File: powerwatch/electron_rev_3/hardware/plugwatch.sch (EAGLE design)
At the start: 121 parts, among them J1 DM3AT-SF-PEJM5, J2 TC2030-JLINK-NL, U1 BGA725L6-ALT, U10 SIP32510, U11 SIP32510, U12 SIP32510, U13 SIP32510, U14 MPU-9250, U15 OPA322AIDBVT, U2 SAFFB1G56KB0F0A, U3 ISL29035, U4 MAX-M8, U5 MAX740XESA, U6 SIP32510, U7 NRF51822QF, U8 OPA322AIDBVT, U9 SIP32510, X1 32.768k, X2 16MHz

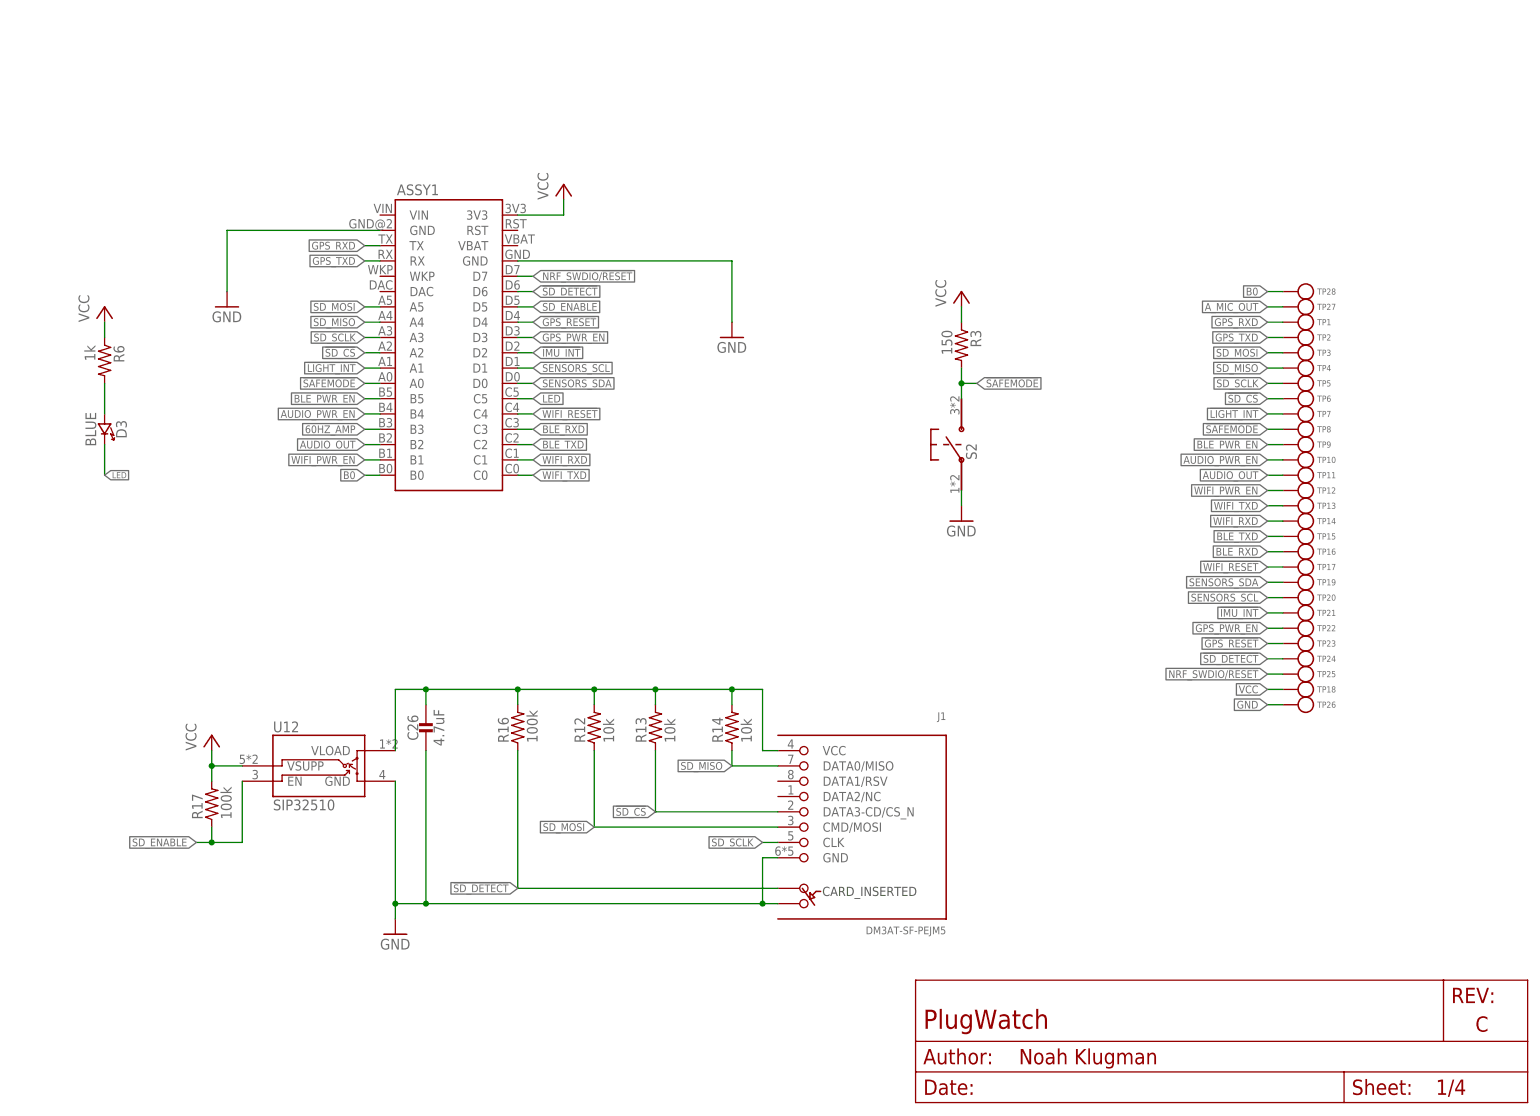
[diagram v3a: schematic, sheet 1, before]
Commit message: added in dip switch, 1-wire serial number, removed rc filter
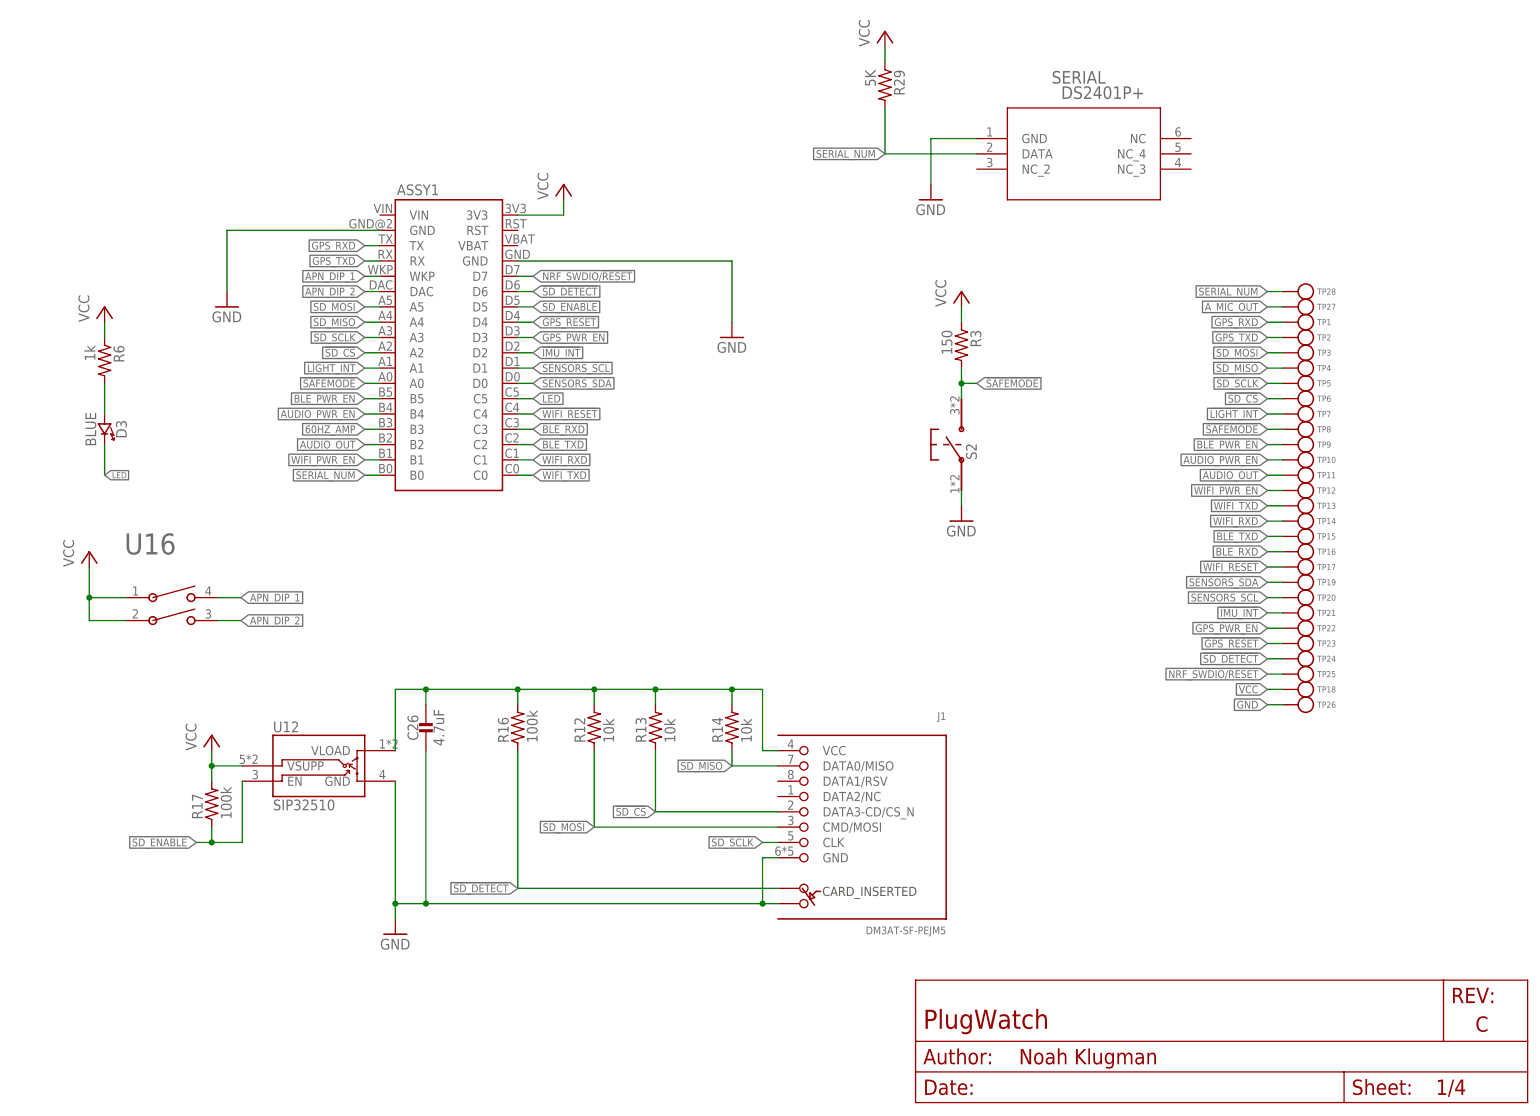
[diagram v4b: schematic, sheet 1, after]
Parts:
- removed C24: 2.2uF, passives:CAP_POL1206
- removed R24: 100k, passives:RESISTOR0603_RES
- added R29: 5K, passives:RESISTOR0402_RES
- added SERIAL: DS2401P+, DS2401P+:DS2401P+
- added U16: 1825057-1, 18250571:1825057-1
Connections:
- removed net B0: ASSY1.B0, TP28.TESTPOINT
- new net APN_DIP_1: ASSY1.WKP, U16.4
- new net APN_DIP_2: ASSY1.DAC, U16.3
- new net SERIAL_NUM: ASSY1.B0, R29.2, SERIAL.DATA, TP28.TESTPOINT
- net A_MIC_OUT: no longer C24.ANODE, R24.2
- net GND: now also SERIAL.GND; no longer R24.1
- net N$7: no longer C24.CATHODE
- net VCC: now also R29.1, U16.1, U16.2
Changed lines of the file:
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@@
 <?xml version="1.0" encoding="utf-8"?>
 <!DOCTYPE eagle SYSTEM "eagle.dtd">
-<eagle version="8.6.3">
+<eagle version="8.5.1">
 <drawing>
 <settings>
@@
 <setting verticaltext="up"/>
 </settings>
-<grid distance="0.1" unitdist="inch" unit="inch" style="lines" multiple="1" display="yes" altdistance="0.05" altunitdist="inch" altunit="inch"/>
+<grid distance="0.1" unitdist="inch" unit="inch" style="lines" multiple="1" display="no" altdistance="0.01" altunitdist="inch" altunit="inch"/>
 <layers>
 <layer number="1" name="Top" color="4" fill="1" visible="no" active="no"/>
@@
 <attribute name="MPN" value="293D225X9016A2TE3"/>
 </part>
-<part name="C24" library="passives" deviceset="CAP_POL" device="1206" value="2.2uF">
-<attribute name="DESCRIPTION" value="CAP TANT 2.2UF 16V 10% 1206"/>
-<attribute name="DIGIKEY" value="718-1131-1-ND"/>
-<attribute name="MANUFACTURER" value="Vishay"/>
-<attribute name="MPN" value="293D225X9016A2TE3"/>
-</part>
 <part name="C25" library="passives" deviceset="CAPACITOR" device="0402_CAP" value="4.7uF">
 <attribute name="DESCRIPTION" value="CAP CER 4.7UF 6.3V X5R 0402"/>
@@
 <part name="GND11" library="supply1" deviceset="GND" device=""/>
 <part name="GND12" library="SparkFun-Aesthetics" deviceset="GND" device=""/>
-<part name="GND13" library="supply1" deviceset="GND" device=""/>
 <part name="GND14" library="supply1" deviceset="GND" device=""/>
 <part name="GND15" library="supply1" deviceset="GND" device=""/>
@@
 </part>
 <part name="R23" library="passives" deviceset="RESISTOR" device="0603_RES" value="100k">
-<attribute name="DESCRIPTION" value="RES SMD 100K OHM 1% 1/10W 0603"/>
-<attribute name="DIGIKEY" value="541-2972-1-ND"/>
-<attribute name="MANUFACTURER" value="Vishay"/>
-<attribute name="MPN" value="CRCW0603100KFKEB"/>
-</part>
-<part name="R24" library="passives" deviceset="RESISTOR" device="0603_RES" value="100k">
 <attribute name="DESCRIPTION" value="RES SMD 100K OHM 1% 1/10W 0603"/>
 <attribute name="DIGIKEY" value="541-2972-1-ND"/>
@@
 <attribute name="MPN" value="8Y-16.000MAAV-T"/>
 </part>
+<part name="SERIAL" library="DS2401P+" deviceset="DS2401P+" device=""/>
+<part name="P+4" library="supply1" deviceset="VCC" device=""/>
+<part name="R29" library="passives" deviceset="RESISTOR" device="0402_RES" value="5K">
+<attribute name="DESCRIPTION" value="RES SMD 150 OHM 1% 1/16W 0402"/>
+<attribute name="DIGIKEY" value="RMCF0402FT150RCT-ND"/>
+<attribute name="MANUFACTURER" value="Stackpole Electronics"/>
+<attribute name="MPN" value="RMCF0402FT150R"/>
+</part>
+<part name="GND41" library="supply1" deviceset="GND" device=""/>
+<part name="U16" library="18250571" deviceset="1825057-1" device=""/>
+<part name="P+6" library="supply1" deviceset="VCC" device=""/>
 </parts>
 <sheets>
@@
 <instance part="TP9" gate="G$1" x="215.9" y="109.22" rot="R180"/>
 <instance part="U12" gate="G$1" x="45.72" y="48.26"/>
+<instance part="SERIAL" gate="A" x="160.02" y="160.02"/>
+<instance part="P+4" gate="VCC" x="147.32" y="177.8"/>
+<instance part="R29" gate="G$1" x="147.32" y="167.64" rot="R270">
+<attribute name="DIGIKEY" x="147.32" y="167.64" size="1.27" layer="96" rot="R270" display="off"/>
+</instance>
+<instance part="GND41" gate="1" x="154.94" y="149.86"/>
+<instance part="U16" gate="A" x="21.336" y="83.82"/>
+<instance part="P+6" gate="VCC" x="15.24" y="91.44"/>
 </instances>
 <busses>
@@
 <wire x1="213.36" y1="132.08" x2="210.82" y2="132.08" width="0.1524" layer="91"/>
 <label x="210.82" y="132.08" size="1.27" layer="95" rot="R180" xref="yes"/>
-</segment>
-</net>
-<net name="B0" class="0">
-<segment>
-<pinref part="TP28" gate="G$1" pin="TESTPOINT"/>
-<wire x1="213.36" y1="134.62" x2="210.82" y2="134.62" width="0.1524" layer="91"/>
-<label x="210.82" y="134.62" size="1.27" layer="95" rot="R180" xref="yes"/>
-</segment>
-<segment>
-<pinref part="ASSY1" gate="A1" pin="B0"/>
-<wire x1="63.5" y1="104.14" x2="60.96" y2="104.14" width="0.1524" layer="91"/>
-<label x="60.96" y="104.14" size="1.27" layer="95" rot="R180" xref="yes"/>
 </segment>
 </net>
@@
 <wire x1="213.36" y1="66.04" x2="210.82" y2="66.04" width="0.1524" layer="91"/>
 <label x="210.82" y="66.04" size="1.27" layer="95" rot="R180" xref="yes"/>
+</segment>
+<segment>
+<pinref part="SERIAL" gate="A" pin="GND"/>
+<pinref part="GND41" gate="1" pin="GND"/>
+<wire x1="162.56" y1="160.02" x2="154.94" y2="160.02" width="0.1524" layer="91"/>
+<wire x1="154.94" y1="160.02" x2="154.94" y2="152.4" width="0.1524" layer="91"/>
 </segment>
 </net>
@@
 <label x="210.82" y="68.58" size="1.27" layer="95" rot="R180" xref="yes"/>
 </segment>
+<segment>
+<pinref part="R29" gate="G$1" pin="1"/>
+<pinref part="P+4" gate="VCC" pin="VCC"/>
+<wire x1="147.32" y1="172.72" x2="147.32" y2="175.26" width="0.1524" layer="91"/>
+</segment>
+<segment>
+<pinref part="U16" gate="A" pin="1"/>
+<wire x1="21.336" y1="83.82" x2="15.24" y2="83.82" width="0.1524" layer="91"/>
+<wire x1="15.24" y1="83.82" x2="15.24" y2="88.9" width="0.1524" layer="91"/>
+<wire x1="15.24" y1="83.82" x2="15.24" y2="80.01" width="0.1524" layer="91"/>
+<wire x1="15.24" y1="80.01" x2="21.336" y2="80.01" width="0.1524" layer="91"/>
+<pinref part="U16" gate="A" pin="2"/>
+<junction x="15.24" y="83.82"/>
+<pinref part="P+6" gate="VCC" pin="VCC"/>
+</segment>
 </net>
 <net name="WIFI_PWR_EN" class="0">
@@
 <wire x1="213.36" y1="99.06" x2="210.82" y2="99.06" width="0.1524" layer="91"/>
 <label x="210.82" y="99.06" size="1.27" layer="95" rot="R180" xref="yes"/>
+</segment>
+</net>
+<net name="APN_DIP_1" class="0">
+<segment>
+<pinref part="ASSY1" gate="A1" pin="WKP"/>
+<wire x1="63.5" y1="137.16" x2="60.96" y2="137.16" width="0.1524" layer="91"/>
+<label x="60.96" y="137.16" size="1.27" layer="95" rot="R180" xref="yes"/>
+</segment>
+<segment>
+<pinref part="U16" gate="A" pin="4"/>
+<wire x1="36.576" y1="83.82" x2="40.386" y2="83.82" width="0.1524" layer="91"/>
+<label x="40.386" y="83.82" size="1.27" layer="95" xref="yes"/>
+</segment>
+</net>
+<net name="APN_DIP_2" class="0">
+<segment>
+<pinref part="ASSY1" gate="A1" pin="DAC"/>
+<wire x1="63.5" y1="134.62" x2="60.96" y2="134.62" width="0.1524" layer="91"/>
+<label x="60.96" y="134.62" size="1.27" layer="95" rot="R180" xref="yes"/>
+</segment>
+<segment>
+<pinref part="U16" gate="A" pin="3"/>
+<wire x1="36.576" y1="80.01" x2="40.386" y2="80.01" width="0.1524" layer="91"/>
+<label x="40.386" y="80.01" size="1.27" layer="95" xref="yes"/>
+</segment>
+</net>
+<net name="SERIAL_NUM" class="0">
+<segment>
+<pinref part="ASSY1" gate="A1" pin="B0"/>
+<wire x1="63.5" y1="104.14" x2="60.96" y2="104.14" width="0.1524" layer="91"/>
+<label x="60.96" y="104.14" size="1.27" layer="95" rot="R180" xref="yes"/>
+</segment>
+<segment>
+<pinref part="TP28" gate="G$1" pin="TESTPOINT"/>
+<wire x1="213.36" y1="134.62" x2="210.82" y2="134.62" width="0.1524" layer="91"/>
+<label x="210.82" y="134.62" size="1.27" layer="95" rot="R180" xref="yes"/>
+</segment>
+<segment>
+<pinref part="SERIAL" gate="A" pin="DATA"/>
+<wire x1="162.56" y1="157.48" x2="147.32" y2="157.48" width="0.1524" layer="91"/>
+<pinref part="R29" gate="G$1" pin="2"/>
+<wire x1="147.32" y1="157.48" x2="147.32" y2="165.1" width="0.1524" layer="91"/>
+<label x="147.32" y="157.48" size="1.27" layer="95" rot="R180" xref="yes"/>
 </segment>
 </net>
@@
 <attribute name="DIGIKEY" x="60.96" y="119.38" size="1.778" layer="96" display="off"/>
 </instance>
-<instance part="C24" gate="G$1" x="106.68" y="137.16" rot="R90">
-<attribute name="DIGIKEY" x="106.68" y="137.16" size="1.778" layer="96" rot="R90" display="off"/>
-</instance>
 <instance part="C28" gate="G$1" x="48.26" y="139.7" rot="R270">
 <attribute name="DIGIKEY" x="48.26" y="139.7" size="1.778" layer="96" rot="R270" display="off"/>
@@
 <instance part="GND11" gate="1" x="53.34" y="109.22"/>
 <instance part="GND12" gate="1" x="91.44" y="33.02"/>
-<instance part="GND13" gate="1" x="114.3" y="109.22"/>
 <instance part="GND14" gate="1" x="76.2" y="109.22"/>
 <instance part="GND15" gate="1" x="40.64" y="109.22"/>
@@
 <attribute name="DIGIKEY" x="53.34" y="120.65" size="1.778" layer="96" rot="R90" display="off"/>
 </instance>
-<instance part="R24" gate="G$1" x="114.3" y="124.46" rot="R90">
-<attribute name="DIGIKEY" x="114.3" y="124.46" size="1.778" layer="96" rot="R90" display="off"/>
-</instance>
 <instance part="R25" gate="G$1" x="78.74" y="154.94" rot="R180">
 <attribute name="DIGIKEY" x="78.74" y="154.94" size="1.778" layer="96" rot="R180" display="off"/>
@@
 <net name="A_MIC_OUT" class="0">
 <segment>
-<pinref part="C24" gate="G$1" pin="ANODE"/>
-<pinref part="R24" gate="G$1" pin="2"/>
 <pinref part="U5" gate="U1" pin="IN"/>
-<wire x1="109.22" y1="137.16" x2="114.3" y2="137.16" width="0.1524" layer="91"/>
-<wire x1="114.3" y1="137.16" x2="114.3" y2="127" width="0.1524" layer="91"/>
-<wire x1="129.54" y1="137.16" x2="114.3" y2="137.16" width="0.1524" layer="91"/>
-<junction x="114.3" y="137.16"/>
+<wire x1="129.54" y1="137.16" x2="104.14" y2="137.16" width="0.1524" layer="91"/>
 <label x="116.84" y="137.16" size="1.016" layer="95" rot="R90" xref="yes"/>
 </segment>
@@
 <wire x1="76.2" y1="38.1" x2="76.2" y2="50.8" width="0.1524" layer="91"/>
 <junction x="68.58" y="38.1"/>
-</segment>
-<segment>
-<pinref part="GND13" gate="1" pin="GND"/>
-<pinref part="R24" gate="G$1" pin="1"/>
-<wire x1="114.3" y1="111.76" x2="114.3" y2="119.38" width="0.1524" layer="91"/>
 </segment>
 <segment>
@@
 <net name="N$7" class="0">
 <segment>
-<pinref part="C24" gate="G$1" pin="CATHODE"/>
 <pinref part="R1" gate="G$1" pin="1"/>
 <wire x1="101.6" y1="137.16" x2="104.14" y2="137.16" width="0.1524" layer="91"/>

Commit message: small changes
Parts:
- renumbered U16 to APN_SWITCH
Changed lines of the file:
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@@
 </part>
 <part name="GND41" library="supply1" deviceset="GND" device=""/>
-<part name="U16" library="18250571" deviceset="1825057-1" device=""/>
+<part name="APN_SWITCH" library="18250571" deviceset="1825057-1" device=""/>
 <part name="P+6" library="supply1" deviceset="VCC" device=""/>
 </parts>
@@
 </instance>
 <instance part="GND41" gate="1" x="154.94" y="149.86"/>
-<instance part="U16" gate="A" x="21.336" y="83.82"/>
+<instance part="APN_SWITCH" gate="A" x="21.336" y="83.82"/>
 <instance part="P+6" gate="VCC" x="15.24" y="91.44"/>
 </instances>
@@
 </segment>
 <segment>
-<pinref part="U16" gate="A" pin="1"/>
+<pinref part="APN_SWITCH" gate="A" pin="1"/>
 <wire x1="21.336" y1="83.82" x2="15.24" y2="83.82" width="0.1524" layer="91"/>
 <wire x1="15.24" y1="83.82" x2="15.24" y2="88.9" width="0.1524" layer="91"/>
 <wire x1="15.24" y1="83.82" x2="15.24" y2="80.01" width="0.1524" layer="91"/>
 <wire x1="15.24" y1="80.01" x2="21.336" y2="80.01" width="0.1524" layer="91"/>
-<pinref part="U16" gate="A" pin="2"/>
+<pinref part="APN_SWITCH" gate="A" pin="2"/>
 <junction x="15.24" y="83.82"/>
 <pinref part="P+6" gate="VCC" pin="VCC"/>
@@
 </segment>
 <segment>
-<pinref part="U16" gate="A" pin="4"/>
+<pinref part="APN_SWITCH" gate="A" pin="4"/>
 <wire x1="36.576" y1="83.82" x2="40.386" y2="83.82" width="0.1524" layer="91"/>
 <label x="40.386" y="83.82" size="1.27" layer="95" xref="yes"/>
@@
 </segment>
 <segment>
-<pinref part="U16" gate="A" pin="3"/>
+<pinref part="APN_SWITCH" gate="A" pin="3"/>
 <wire x1="36.576" y1="80.01" x2="40.386" y2="80.01" width="0.1524" layer="91"/>
 <label x="40.386" y="80.01" size="1.27" layer="95" xref="yes"/>

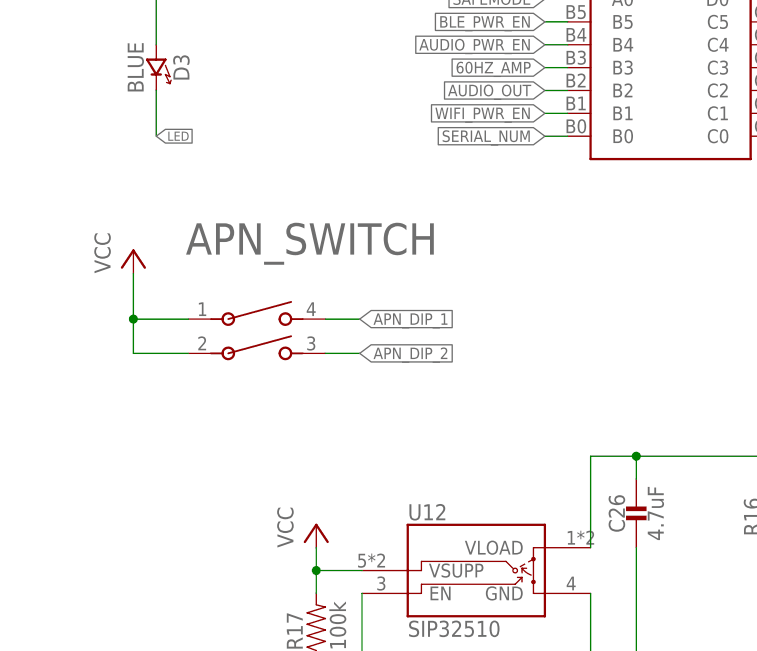
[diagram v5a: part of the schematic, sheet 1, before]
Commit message: fixed library parts and added pulldowns
specifically
    - made sure origins were at the center of the part
    - fixed ds2401p+ lan pattern to match maxim spec
    - changed text ratios to 12
    - changed attribute fields to match rest of BOM
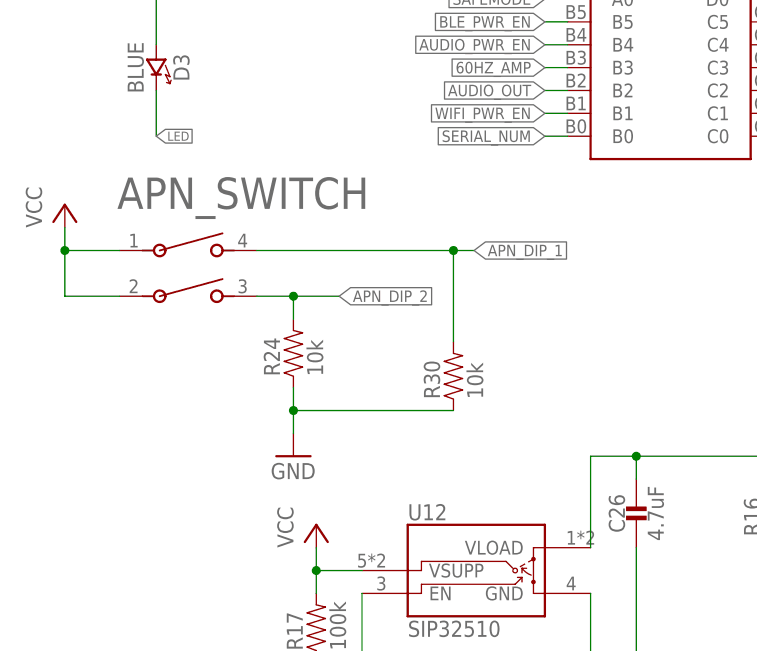
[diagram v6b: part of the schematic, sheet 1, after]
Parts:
- added R24, R30: 10k, passives:RESISTOR0402_RES
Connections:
- net APN_DIP_1: now also R30.2
- net APN_DIP_2: now also R24.2
- net GND: now also R24.1, R30.1
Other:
- moved on the sheet: APN_SWITCH
